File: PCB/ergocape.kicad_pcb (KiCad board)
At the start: 2 copper layers, 183.2 x 140.8 mm, 86 parts, among them J1 AudioJack4, J2 AudioJack4, M1 >VALUE

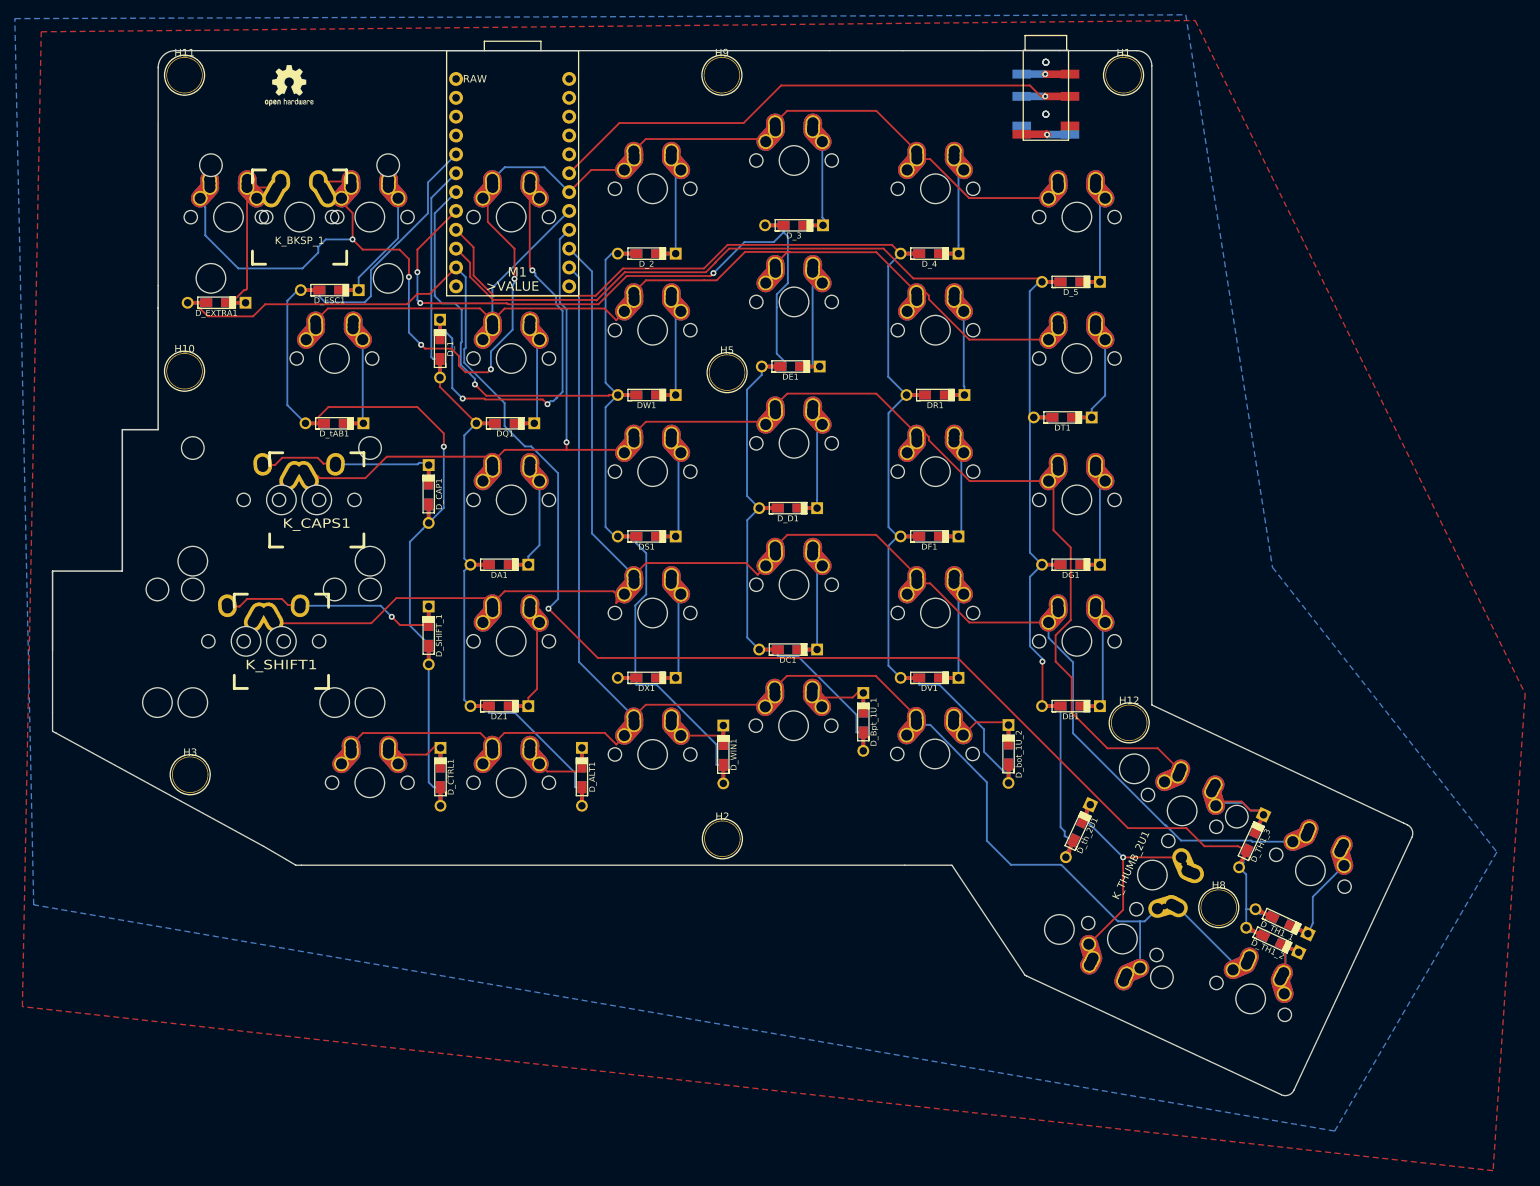
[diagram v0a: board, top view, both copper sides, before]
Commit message: cleanup some wiring, check diode placement
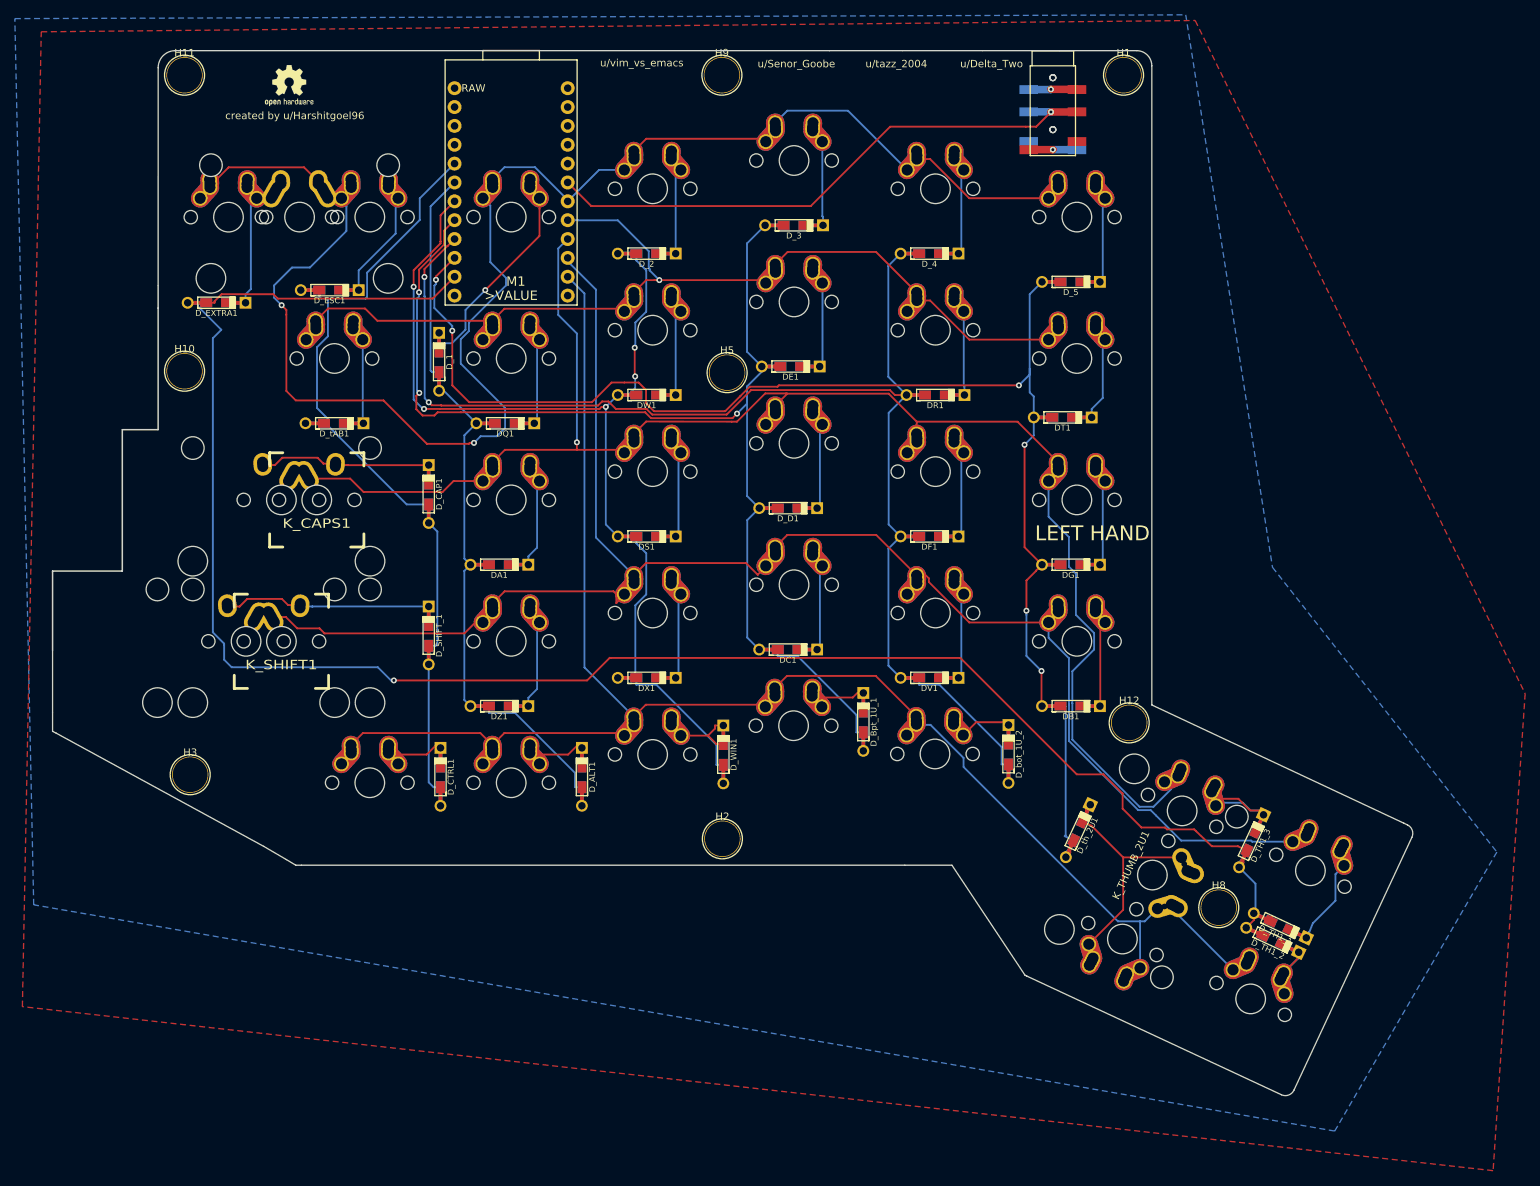
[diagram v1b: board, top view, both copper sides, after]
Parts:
- K_BKSP_1: moved to B.Cu
- moved J1 2.29 mm to (157.1, 19.3)
- moved J2 2.29 mm to (157.1, 19.3)
- moved D_1 1.78 mm to (74.4, 59.2)
- moved M1 1.26 mm to (84.1, 35.0)
- moved D_TH1_1 0.60 mm to (187.7, 135.1)
- turned K_BKSP_1 to 180 degrees
- renumbered REF** to log_bsilk1, REF** to logo_fsilk
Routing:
- net /COL7: track 224.9 -> 261.0 mm
- net Net-(D_1-Pad1): track 64.2 -> 35.6 mm, vias 3 -> 1
- net /COL5: track 175.7 -> 195.3 mm, vias 0 -> 2
- net /COL6: track 192.8 -> 212.4 mm, vias 1 -> 6
- net /ROW1: track 218.0 -> 237.4 mm, vias 5 -> 2
- net /COL1: track 145.6 -> 128.3 mm, vias 1 -> 0
- net /ROW2: track 158.2 -> 146.8 mm, vias 0 -> 1
- net /ROW3: track 219.8 -> 228.3 mm
- net /ROW5: track 245.0 -> 238.1 mm
- net Net-(D_TH1_2-Pad1): track 13.9 -> 20.1 mm
- net /COL4: track 173.1 -> 178.5 mm
- net /COL3: track 156.4 -> 160.5 mm, vias 1 -> 5
- net Net-(D_TH1_1-Pad1): track 21.4 -> 17.9 mm
- net Net-(D_WIN1-Pad1): track 15.1 -> 17.4 mm
- net /SERIAL: track 76.1 -> 78.2 mm
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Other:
- board text added: "LEFT HAND"
- board text added: "RIGHT HAND"
- board text added: "created by u/Harshitgoel96"
- board text added: "u/Delta_Two"
- board text added: "u/Senor_Goobe"
- board text added: "u/tazz_2004"
- board text added: "u/vim_vs_emacs"

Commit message: fix pro micro footprint
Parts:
- moved K_THUMB_1U_4 0.22 mm to (174.6, 119.9)
- moved D_TH1_1 0.22 mm to (187.8, 135.3)
- moved D_TH1_3 0.22 mm to (183.9, 123.9)
- moved D_th_2U1 0.22 mm to (160.6, 122.6)
- moved D_TH1_2 0.22 mm to (186.8, 137.3)
- moved K_THUMB_1U_3 0.22 mm to (166.6, 137.1)
- moved K_TH_1U_1 0.22 mm to (191.9, 127.9)
- moved H8 0.22 mm to (179.6, 132.9)
- moved K_THUMB_2U1 0.22 mm to (170.6, 128.5)
- moved K_TH_1U_2 0.22 mm to (183.9, 145.2)
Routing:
- net /ROW5: track 238.1 -> 245.2 mm
- net Net-(D_th_2U1-Pad1): track 42.4 -> 47.5 mm
- net Net-(D_TH1_2-Pad1): track 20.1 -> 16.3 mm
- net /COL7: track 261.0 -> 264.4 mm, vias 1 -> 2
- net /COL6: track 212.4 -> 214.5 mm, vias 6 -> 5
- net Net-(D_CAP1-Pad1): track 28.1 -> 30.1 mm
- net /ROW1: track 237.4 -> 239.1 mm, vias 2 -> 3
- net /ROW3: track 228.3 -> 227.0 mm
- net /ROW4: track 243.3 -> 243.5 mm, vias 0 -> 1
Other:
- board size 183.2 x 140.8 mm -> 186.4 x 145 mm
- board text added: ""Tazz""
- board text added: "captn3m0"
- board text removed: "u/tazz_2004"
- board text removed: "u/vim_vs_emacs"
